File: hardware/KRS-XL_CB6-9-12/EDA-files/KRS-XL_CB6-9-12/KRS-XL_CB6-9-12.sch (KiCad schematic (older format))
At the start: 55 parts, among them J1 KNX / GND, J2 Conn_02x10_Odd_Even, J3 KNX / GND, SW1 SW_Push_Dual, SW10 SW_Push_Dual, SW11 SW_Push_Dual, SW12 SW_Push_Dual, SW13 SW_Push_Dual, SW14 SW_Push_Dual, SW15 SW_Push_Dual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

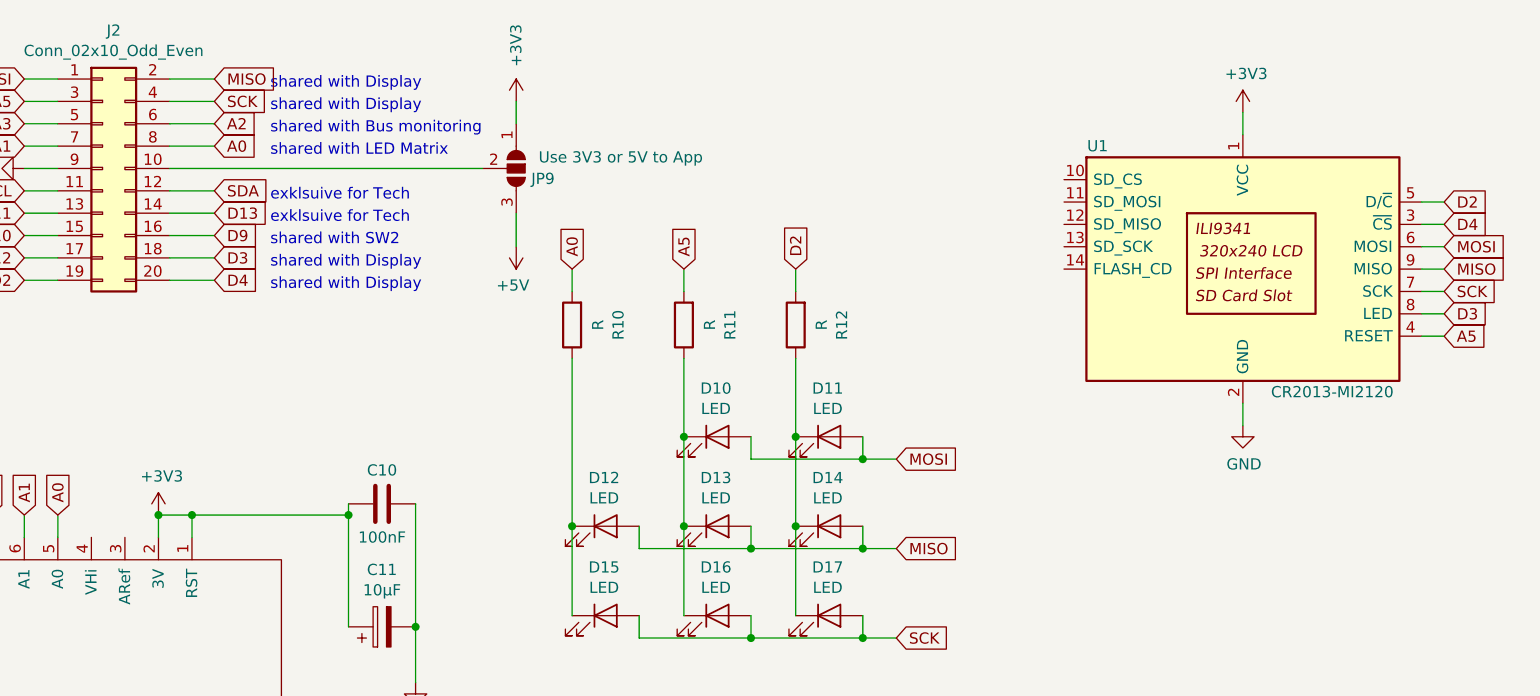
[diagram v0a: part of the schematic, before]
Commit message: worked on V01.01 - RST of ItsyBitsy disconnected from 3v3
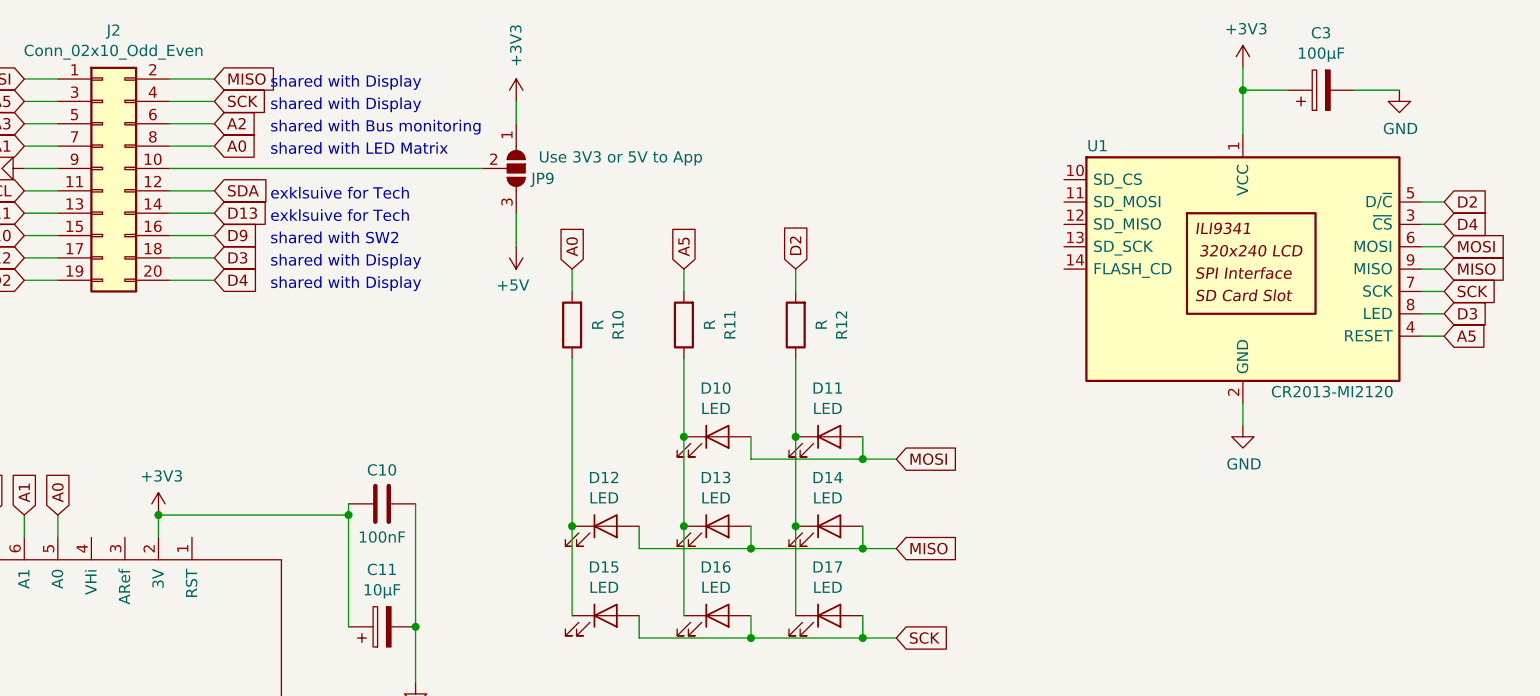
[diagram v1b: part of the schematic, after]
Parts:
- added C3: 100µF, Capacitor_SMD:CP_Elec_5x5.3, symbol Device:CP
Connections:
- net +3V3: now also C3.1; no longer GN2.1 (RST)
- net GND: now also C3.2
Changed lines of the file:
@@
 EESchema Schematic File Version 4
-LIBS:Controllerboard_9TE-cache
+LIBS:KRS-XL_CB6-9-12-cache
 EELAYER 30 0
 EELAYER END
@@
 Sheet 1 1
 Title "KRS-XL CB6-9-12"
-Date "2019-11-08"
-Rev "V01.00"
-Comp "SirSydom KNX Labs"
-Comment1 ""
-Comment2 "com@sirsydom.de"
+Date "2020-01-10"
+Rev "V01.01_work"
+Comp "KNX Makerstuff"
+Comment1 "by SirSydom <com@sirsydom.de>"
+Comment2 ""
 Comment3 ""
-Comment4 ""
+Comment4 "https://gitlab.com/knx-makerstuff/knx-rail-system-xl"
 $EndDescr
 $Comp
@@
 	1    0    0    -1
 $EndComp
-Wire Wire Line
-	10050 1000 10050 1100
 Wire Wire Line
 	10050 2300 10050 2400
@@
 	0    -1   -1   0
 $EndComp
-Wire Wire Line
-	5200 2800 5350 2800
 Connection ~ 5200 2800
 Wire Wire Line
@@
 L power:+3V3 #PWR0111
 U 1 1 5DD38741
-P 10050 1000
-F 0 "#PWR0111" H 10050 850 50  0001 C CNN
-F 1 "+3V3" H 10065 1173 50  0000 C CNN
-F 2 "" H 10050 1000 50  0001 C CNN
-F 3 "" H 10050 1000 50  0001 C CNN
-	1    10050 1000
+P 10050 800
+F 0 "#PWR0111" H 10050 650 50  0001 C CNN
+F 1 "+3V3" H 10065 973 50  0000 C CNN
+F 2 "" H 10050 800 50  0001 C CNN
+F 3 "" H 10050 800 50  0001 C CNN
+	1    10050 800
 	1    0    0    -1
 $EndComp
@@
 	6350 3300 6350 3550
 Wire Wire Line
-	5350 2900 5350 2800
-Connection ~ 5350 2800
-Wire Wire Line
-	5350 2800 6050 2800
+	5200 2800 6050 2800
+$Comp
+L Device:CP C3
+U 1 1 5E19FBD3
+P 10400 900
+F 0 "C3" V 10655 900 50  0000 C CNN
+F 1 "100µF" V 10564 900 50  0000 C CNN
+F 2 "Capacitor_SMD:CP_Elec_5x5.3" H 10438 750 50  0001 C CNN
+F 3 "~" H 10400 900 50  0001 C CNN
+	1    10400 900
+	0    -1   -1   0
+$EndComp
+Wire Wire Line
+	10050 800  10050 900
+Wire Wire Line
+	10250 900  10050 900
+Connection ~ 10050 900
+Wire Wire Line
+	10050 900  10050 1100
+$Comp
+L power:GND #PWR03
+U 1 1 5E1CF269
+P 10750 900
+F 0 "#PWR03" H 10750 650 50  0001 C CNN
+F 1 "GND" H 10755 727 50  0000 C CNN
+F 2 "" H 10750 900 50  0001 C CNN
+F 3 "" H 10750 900 50  0001 C CNN
+	1    10750 900
+	1    0    0    -1
+$EndComp
+Wire Wire Line
+	10550 900  10750 900
 $EndSCHEMATC

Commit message: V01.01
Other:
- note added: "C3 not in Layout"
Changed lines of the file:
@@
 Sheet 1 1
 Title "KRS-XL CB6-9-12"
-Date "2020-01-10"
-Rev "V01.01_work"
+Date "2022-01-22"
+Rev "V01.01"
 Comp "KNX Makerstuff"
 Comment1 "by SirSydom <com@sirsydom.de>"
@@
 Wire Wire Line
 	10550 900  10750 900
+Text Notes 10550 650  0    50   ~ 0
+C3 not in Layout
 $EndSCHEMATC
